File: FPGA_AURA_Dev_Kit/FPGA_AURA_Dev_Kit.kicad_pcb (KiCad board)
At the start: 2 copper layers, 100 x 80 mm, 11 parts, among them J1 Barrel_Jack, J2 Conn_Coaxial_Small, J3 Conn_Coaxial_Small, J4 AVR-JTAG-10, J5 Conn_02x10_Odd_Even, J6 Conn_02x10_Odd_Even

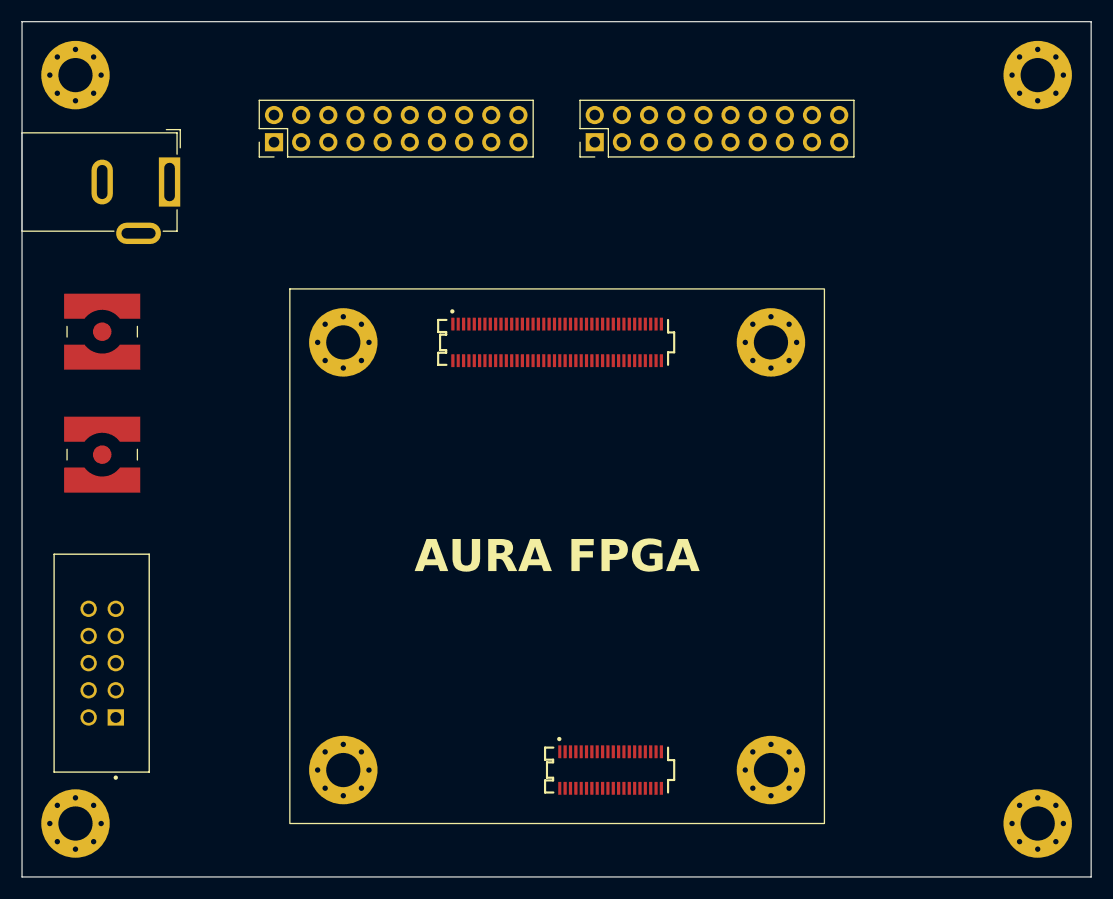
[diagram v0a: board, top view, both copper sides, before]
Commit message: Continued dev kit. Moving focus to ordering FPGA prior to finishing dev kit.
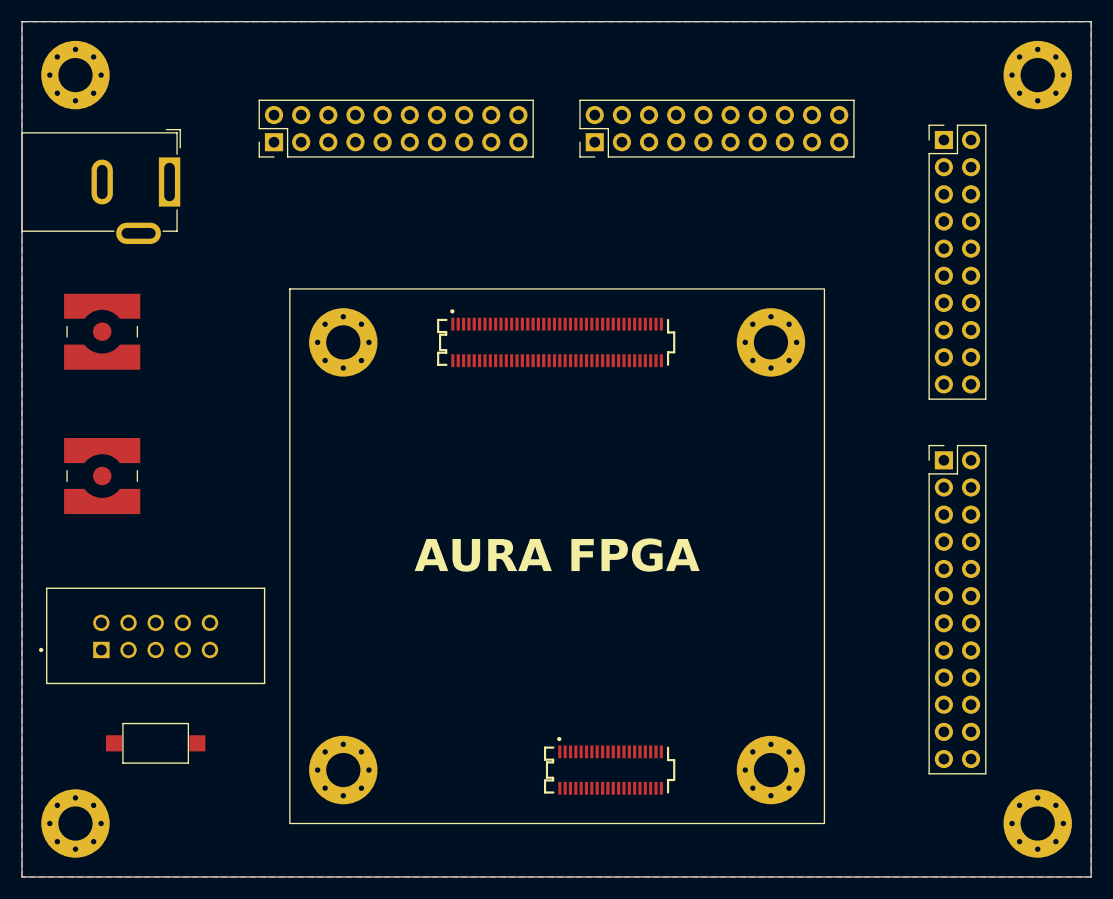
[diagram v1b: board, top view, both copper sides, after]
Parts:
- added J7: Conn_02x10_Odd_Even, Connector_PinHeader_2.54mm:PinHeader_2x10_P2.54mm_Vertical, F.Cu at (186.2, 61.1)
- added J8: Conn_02x12_Odd_Even, Connector_PinHeader_2.54mm:PinHeader_2x12_P2.54mm_Vertical, F.Cu at (186.2, 91.0)
- added SW1: SW_Push_Open, Button_Switch_SMD:SW_SPST_CK_RS282G05A3, F.Cu at (112.5, 117.5)
- moved J5 30.0 mm to (123.6, 61.3)
- moved J6 30.0 mm to (153.6, 61.3)
- moved J4 5.59 mm to (112.5, 107.5), turned to 0 degrees
- moved J2 2.00 mm to (107.5, 92.5)
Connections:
- J6 pad 10: ETH_0_RXD_1 -> ETH_1_RXD_1
- J6 pad 11: ETH_0_TX_CLK -> ETH_1_TX_CLK
- J6 pad 12: ETH_0_RXD_3 -> ETH_1_RXD_3
- J6 pad 13: ETH_0_TXD_0 -> ETH_1_TXD_0
- J6 pad 14: ETH_0_TX_EN -> ETH_1_TX_EN
- J6 pad 15: ETH_0_TXD_2 -> ETH_1_TXD_2
- J6 pad 16: ETH_0_TXD_1 -> ETH_1_TXD_1
- J6 pad 17: PHY_0_RST -> PHY_1_RST
- J6 pad 18: ETH_0_TXD_3 -> ETH_1_TXD_3
- J6 pad 3: ETH_0_RX_DV -> ETH_1_RX_DV
- J6 pad 4: ETH_0_RX_CLK -> ETH_1_RX_CLK
- J6 pad 5: ETH_0_RX_ER -> ETH_1_RX_ER
- J6 pad 6: ETH_0_CRS -> ETH_1_CRS
- J6 pad 7: ETH_0_RXD_0 -> ETH_1_RXD_0
- J6 pad 8: ETH_0_COL -> ETH_1_COL
- J6 pad 9: ETH_0_RXD_2 -> ETH_1_RXD_2
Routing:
- added copper zone on B.Cu, net GND
- added copper zone on F.Cu, net GND
- added copper zone on In1.Cu, net GND
- added copper zone on In2.Cu, net GND
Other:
- copper layers 2 -> 4
